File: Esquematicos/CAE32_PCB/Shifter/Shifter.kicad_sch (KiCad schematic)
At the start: 0 parts

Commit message: add: diseño de esquemático básico usando el microcontrolador rp2040
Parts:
- added J1: RJ45, Connector_RJ:RJ45_Amphenol_RJHSE538X, symbol Connector:RJ45
- added J2: USB_C_Receptacle_USB2.0, Connector_USB:USB_C_Receptacle_G-Switch_GT-USB-7010ASV, symbol Connector:USB_C_Receptacle_USB2.0
- added U1: RP2040, Package_DFN_QFN:QFN-56-1EP_7x7mm_P0.4mm_EP3.2x3.2mm, symbol MCU_RaspberryPi:RP2040
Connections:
- new net: U1.1 (IOVDD), U1.10 (IOVDD), U1.22 (IOVDD), U1.33 (IOVDD), U1.42 (IOVDD), U1.49 (IOVDD)
- new net: U1.23 (DVDD), U1.50 (DVDD)
- new net: J2.A1 (GND), J2.A12 (GND), J2.B1 (GND), J2.B12 (GND)
- new net: J2.A4 (VBUS), J2.A9 (VBUS), J2.B4 (VBUS), J2.B9 (VBUS)
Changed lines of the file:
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@@
 (kicad_sch (version 20211123) (generator eeschema)
   (paper "A4")
+  (symbol (lib_id "MCU_RaspberryPi:RP2040") (at 72.39 74.295 0) (unit 1)
+    (in_bom yes) (on_board yes) (fields_autoplaced)
+    (property "Reference" "U1" (id 0) (at 74.4094 119.38 0)
+      (effects (font (size 1.27 1.27)) (justify left))
+    )
+    (property "Value" "RP2040" (id 1) (at 74.4094 121.92 0)
+      (effects (font (size 1.27 1.27)) (justify left))
+    )
+    (property "Footprint" "Package_DFN_QFN:QFN-56-1EP_7x7mm_P0.4mm_EP3.2x3.2mm" (id 2) (at 72.39 74.295 0)
+      (effects (font (size 1.27 1.27)) hide)
+    )
+    (property "Datasheet" "https://datasheets.raspberrypi.com/rp2040/rp2040-datasheet.pdf" (id 3) (at 72.39 74.295 0)
+      (effects (font (size 1.27 1.27)) hide)
+    )
+    (pin "1")
+    (pin "10")
+    (pin "11")
+    (pin "12")
+    (pin "13")
+    (pin "14")
+    (pin "15")
+    (pin "16")
+    (pin "17")
+    (pin "18")
+    (pin "19")
+    (pin "2")
+    (pin "20")
+    (pin "21")
+    (pin "22")
+    (pin "23")
+    (pin "24")
+    (pin "25")
+    (pin "26")
+    (pin "27")
+    (pin "28")
+    (pin "29")
+    (pin "3")
+    (pin "30")
+    (pin "31")
+    (pin "32")
+    (pin "33")
+    (pin "34")
+    (pin "35")
+    (pin "36")
+    (pin "37")
+    (pin "38")
+    (pin "39")
+    (pin "4")
+    (pin "40")
+    (pin "41")
+    (pin "42")
+    (pin "43")
+    (pin "44")
+    (pin "45")
+    (pin "46")
+    (pin "47")
+    (pin "48")
+    (pin "49")
+    (pin "5")
+    (pin "50")
+    (pin "51")
+    (pin "52")
+    (pin "53")
+    (pin "54")
+    (pin "55")
+    (pin "56")
+    (pin "57")
+    (pin "6")
+    (pin "7")
+    (pin "8")
+    (pin "9")
+  )
+  (symbol (lib_id "Connector:RJ45") (at 213.995 41.275 0) (unit 1)
+    (in_bom yes) (on_board yes) (fields_autoplaced)
+    (property "Reference" "J1" (id 0) (at 213.995 22.86 0))
+    (property "Value" "RJ45" (id 1) (at 213.995 25.4 0))
+    (property "Footprint" "Connector_RJ:RJ45_Amphenol_RJHSE538X" (id 2) (at 213.995 40.64 90)
+      (effects (font (size 1.27 1.27)) hide)
+    )
+    (property "Datasheet" "~" (id 3) (at 213.995 40.64 90)
+      (effects (font (size 1.27 1.27)) hide)
+    )
+    (pin "1")
+    (pin "2")
+    (pin "3")
+    (pin "4")
+    (pin "5")
+    (pin "6")
+    (pin "7")
+    (pin "8")
+  )
+  (symbol (lib_id "Connector:USB_C_Receptacle_USB2.0") (at 219.075 83.82 0) (unit 1)
+    (in_bom yes) (on_board yes) (fields_autoplaced)
+    (property "Reference" "J2" (id 0) (at 219.075 60.96 0))
+    (property "Value" "USB_C_Receptacle_USB2.0" (id 1) (at 219.075 63.5 0))
+    (property "Footprint" "Connector_USB:USB_C_Receptacle_G-Switch_GT-USB-7010ASV" (id 2) (at 222.885 83.82 0)
+      (effects (font (size 1.27 1.27)) hide)
+    )
+    (property "Datasheet" "https://www.usb.org/sites/default/files/documents/usb_type-c.zip" (id 3) (at 222.885 83.82 0)
+      (effects (font (size 1.27 1.27)) hide)
+    )
+    (pin "A1")
+    (pin "A12")
+    (pin "A4")
+    (pin "A5")
+    (pin "A6")
+    (pin "A7")
+    (pin "A8")
+    (pin "A9")
+    (pin "B1")
+    (pin "B12")
+    (pin "B4")
+    (pin "B5")
+    (pin "B6")
+    (pin "B7")
+    (pin "B8")
+    (pin "B9")
+    (pin "S1")
+  )
   (sheet_instances
     (path "/" (page "1"))
   )
+  (symbol_instances
+    (path "/d83f6367-21e4-44e4-96ad-633fe7714391"
+      (reference "J1") (unit 1) (value "RJ45") (footprint "Connector_RJ:RJ45_Amphenol_RJHSE538X")
+    )
+    (path "/df924866-e23e-469c-b006-990089a46aff"
+      (reference "J2") (unit 1) (value "USB_C_Receptacle_USB2.0") (footprint "Connector_USB:USB_C_Receptacle_G-Switch_GT-USB-7010ASV")
+    )
+    (path "/5661b59b-f47f-4f9f-b3df-14e1858267dc"
+      (reference "U1") (unit 1) (value "RP2040") (footprint "Package_DFN_QFN:QFN-56-1EP_7x7mm_P0.4mm_EP3.2x3.2mm")
+    )
+  )
 )

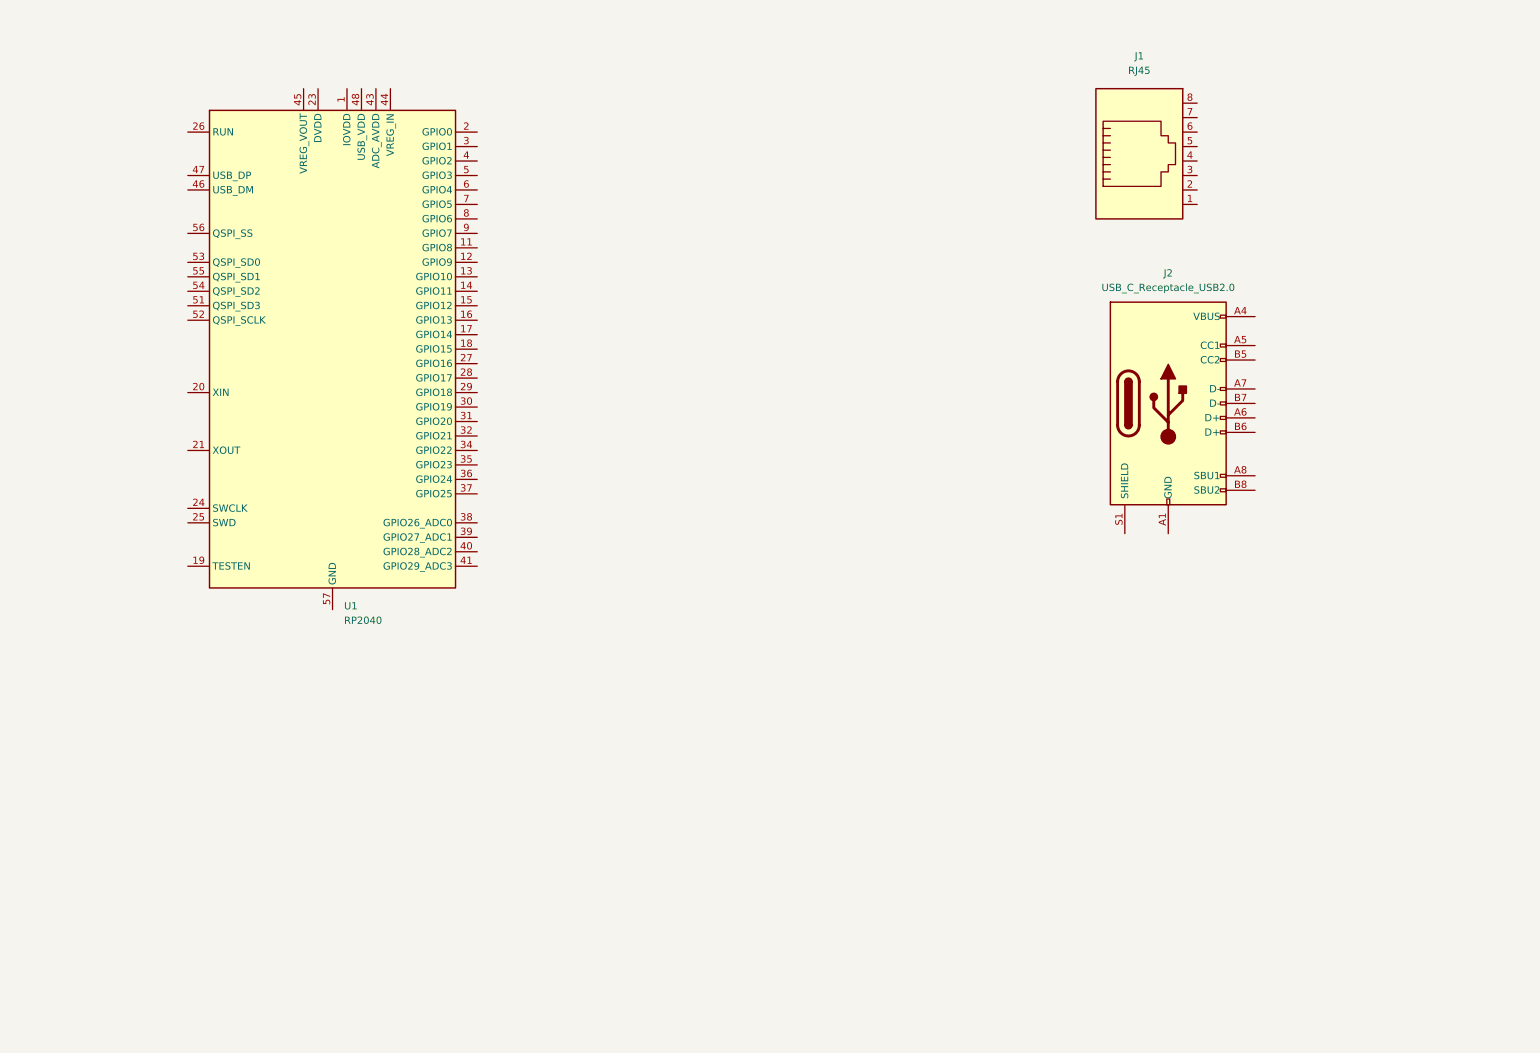
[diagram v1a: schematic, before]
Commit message: update: se enruta completamente la pcb, aunque aun necesario un análisis posterior, ademas de agregar huellas e imagen de la pcb completa
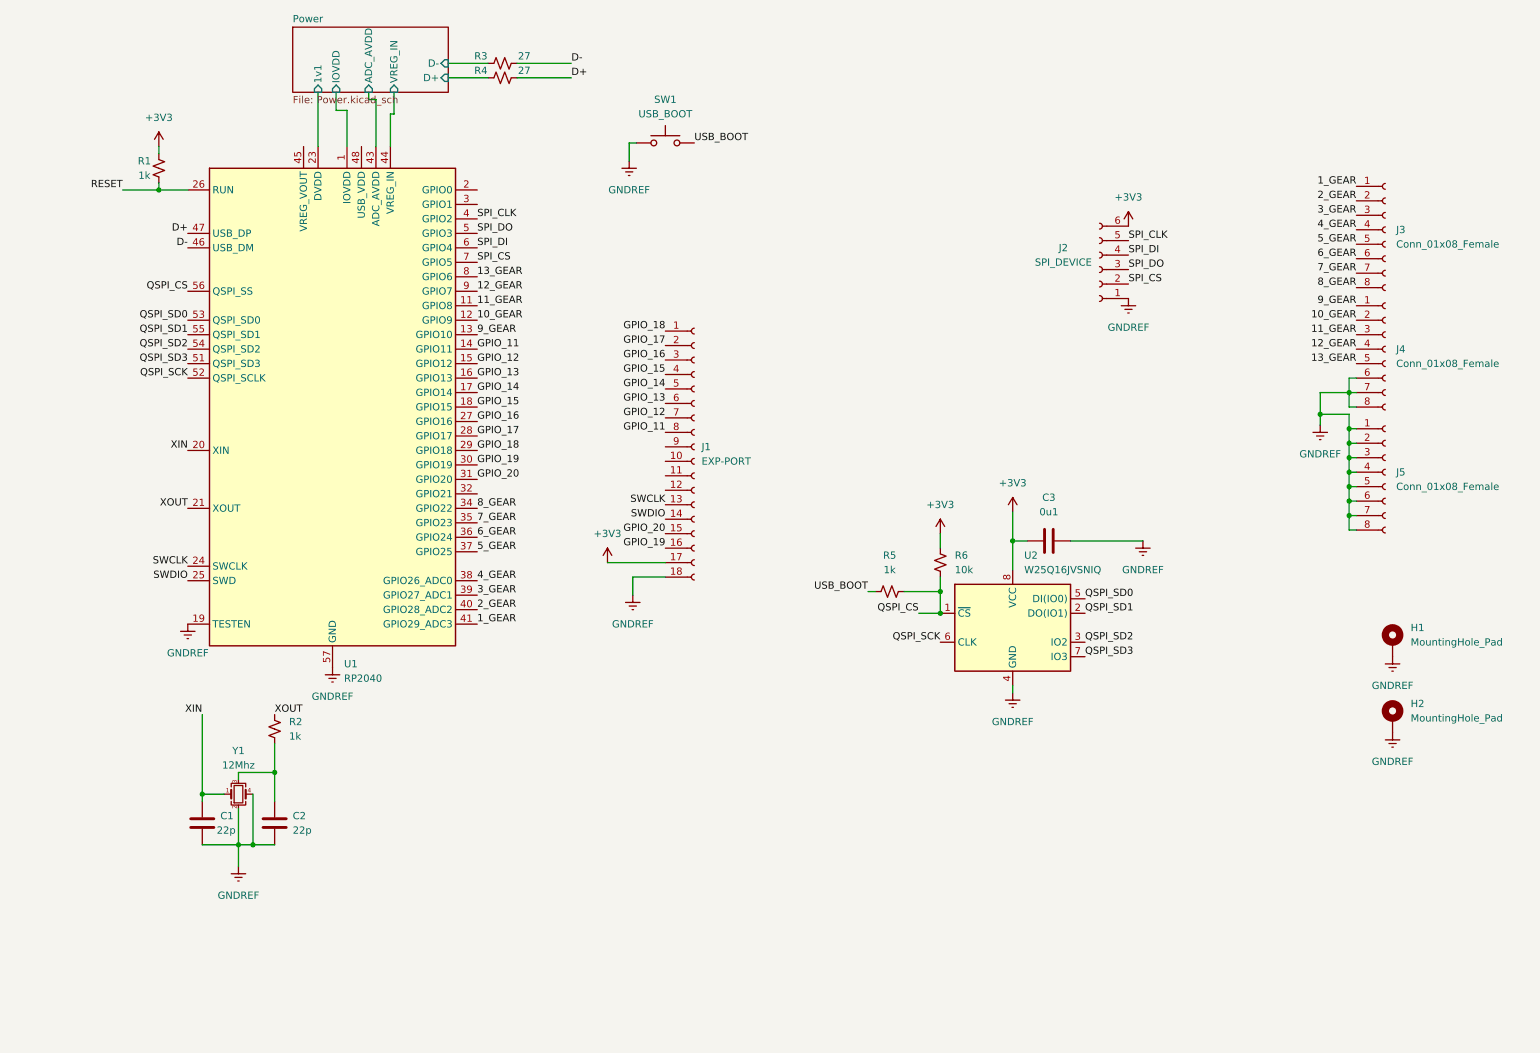
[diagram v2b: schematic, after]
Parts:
- removed J1: RJ45, Connector_RJ:RJ45_Amphenol_RJHSE538X, symbol Connector:RJ45
- removed J2: USB_C_Receptacle_USB2.0, Connector_USB:USB_C_Receptacle_G-Switch_GT-USB-7010ASV, symbol Connector:USB_C_Receptacle_USB2.0
- added C1, C2: 22p, Capacitor_SMD:C_0603_1608Metric_Pad1.08x0.95mm_HandSolder, symbol Device:C
- added C3: 0u1, Capacitor_SMD:C_0603_1608Metric_Pad1.08x0.95mm_HandSolder, symbol Device:C
- added H1, H2: MountingHole_Pad, MountingHole:MountingHole_2.7mm_M2.5_Pad_Via, symbol Mechanical:MountingHole_Pad
- added J1: EXP-PORT, shifter:BM28B0-6-16DS, symbol Connector:Conn_01x18_Female
- added J2: SPI_DEVICE, Connector_PinSocket_2.54mm:PinSocket_2x03_P2.54mm_Vertical, symbol Connector:Conn_01x06_Female
- added J3, J4, J5: Conn_01x08_Female, shifter:shi, symbol Connector:Conn_01x08_Female
- added R1, R2, R5: 1k, Resistor_SMD:R_0603_1608Metric_Pad0.98x0.95mm_HandSolder, symbol Device:R_Small_US
- added R3, R4: 27, Resistor_SMD:R_0603_1608Metric_Pad0.98x0.95mm_HandSolder, symbol Device:R_Small_US
- added R6: 10k, Resistor_SMD:R_0603_1608Metric_Pad0.98x0.95mm_HandSolder, symbol Device:R_Small_US
- added SW1: USB_BOOT, Button_Switch_SMD:SW_Push_SPST_NO_Alps_SKRK, symbol Switch:SW_Push
- added U2: W25Q16JVSNIQ, Package_SO:SOIC-8_5.23x5.23mm_P1.27mm, symbol Memory_Flash:W25Q128JVS
- added Y1: 12Mhz, Crystal:Crystal_SMD_3225-4Pin_3.2x2.5mm, symbol Device:Crystal_GND23_Small
- U1: Vendor (none) -> C2040
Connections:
- net Power/IOVDD: now reaches U1.1 (IOVDD), U1.10 (IOVDD), U1.22 (IOVDD), U1.33 (IOVDD), U1.42 (IOVDD), U1.49 (IOVDD)
- net 11_GEAR: now reaches U1.11 (GPIO8)
- net 11_GEAR: now also J4.3 (Pin_3)
- net 10_GEAR: now reaches U1.12 (GPIO9)
- net 10_GEAR: now also J4.2 (Pin_2)
- net 9_GEAR: now reaches U1.13 (GPIO10)
- net 9_GEAR: now also J4.1 (Pin_1)
- net GPIO_11: now reaches U1.14 (GPIO11)
- net GPIO_11: now also J1.8 (Pin_8)
- net GPIO_12: now reaches U1.15 (GPIO12)
- net GPIO_12: now also J1.7 (Pin_7)
- net GPIO_13: now reaches U1.16 (GPIO13)
- net GPIO_13: now also J1.6 (Pin_6)
- net GPIO_14: now reaches U1.17 (GPIO14)
- net GPIO_14: now also J1.5 (Pin_5)
- net GPIO_15: now reaches U1.18 (GPIO15)
- net GPIO_15: now also J1.4 (Pin_4)
- net GNDREF: now reaches U1.19 (TESTEN)
- net GNDREF: now also U1.57 (GND), C1.2, C2.2, C3.2, H1.1, H2.1, J1.18 (Pin_18), J2.1 (Pin_1), J4.6 (Pin_6), J4.7 (Pin_7), J4.8 (Pin_8), J5.1 (Pin_1), J5.2 (Pin_2), J5.3 (Pin_3), J5.4 (Pin_4), J5.5 (Pin_5), J5.6 (Pin_6), J5.7 (Pin_7), J5.8 (Pin_8), SW1.1, U2.4 (GND), Y1.2, Y1.4
- net XIN: now reaches U1.20 (XIN)
- net XIN: now also C1.1, Y1.1
- net XOUT: now reaches U1.21 (XOUT)
- net XOUT: now also R2.1
- net Power/1v1: now reaches U1.23 (DVDD), U1.50 (DVDD)
- net SWCLK: now reaches U1.24 (SWCLK)
- net SWCLK: now also J1.13 (Pin_13)
- net SWDIO: now reaches U1.25 (SWD)
- net SWDIO: now also J1.14 (Pin_14)
- net RESET: now reaches U1.26 (RUN)
- net RESET: now also R1.2
- net GPIO_16: now reaches U1.27 (GPIO16)
- net GPIO_16: now also J1.3 (Pin_3)
- net GPIO_17: now reaches U1.28 (GPIO17)
- net GPIO_17: now also J1.2 (Pin_2)
- net GPIO_18: now reaches U1.29 (GPIO18)
- net GPIO_18: now also J1.1 (Pin_1)
- net GPIO_19: now reaches U1.30 (GPIO19)
- net GPIO_19: now also J1.16 (Pin_16)
- net GPIO_20: now reaches U1.31 (GPIO20)
- net GPIO_20: now also J1.15 (Pin_15)
- net 8_GEAR: now reaches U1.34 (GPIO22)
- net 8_GEAR: now also J3.8 (Pin_8)
- net 7_GEAR: now reaches U1.35 (GPIO23)
- net 7_GEAR: now also J3.7 (Pin_7)
- net 6_GEAR: now reaches U1.36 (GPIO24)
- net 6_GEAR: now also J3.6 (Pin_6)
- net 5_GEAR: now reaches U1.37 (GPIO25)
- net 5_GEAR: now also J3.5 (Pin_5)
- net 4_GEAR: now reaches U1.38 (GPIO26_ADC0)
- net 4_GEAR: now also J3.4 (Pin_4)
- net 3_GEAR: now reaches U1.39 (GPIO27_ADC1)
- net 3_GEAR: now also J3.3 (Pin_3)
- net SPI_CLK: now reaches U1.4 (GPIO2)
- net SPI_CLK: now also J2.5 (Pin_5)
- net 2_GEAR: now reaches U1.40 (GPIO28_ADC2)
- net 2_GEAR: now also J3.2 (Pin_2)
- net 1_GEAR: now reaches U1.41 (GPIO29_ADC3)
- net 1_GEAR: now also J3.1 (Pin_1)
- net Power/ADC_AVDD: now reaches U1.43 (ADC_AVDD)
- net Power/VREG_IN: now reaches U1.44 (VREG_IN)
- net D-: now reaches U1.46 (USB_DM)
- net D-: now also R3.1
- net D+: now reaches U1.47 (USB_DP)
- net D+: now also R4.1
- net SPI_DO: now reaches U1.5 (GPIO3)
- net SPI_DO: now also J2.3 (Pin_3)
- net QSPI_SD3: now reaches U1.51 (QSPI_SD3)
- net QSPI_SD3: now also U2.7 (IO3)
- net QSPI_SCK: now reaches U1.52 (QSPI_SCLK)
- net QSPI_SCK: now also U2.6 (CLK)
- net QSPI_SD0: now reaches U1.53 (QSPI_SD0)
- net QSPI_SD0: now also U2.5 (DI(IO0))
- net QSPI_SD2: now reaches U1.54 (QSPI_SD2)
- net QSPI_SD2: now also U2.3 (IO2)
- net QSPI_SD1: now reaches U1.55 (QSPI_SD1)
- net QSPI_SD1: now also U2.2 (DO(IO1))
- net QSPI_CS: now reaches U1.56 (QSPI_SS)
- net QSPI_CS: now also R5.2, R6.1, U2.1 (~{CS})
- net SPI_DI: now reaches U1.6 (GPIO4)
- net SPI_DI: now also J2.4 (Pin_4)
- net SPI_CS: now reaches U1.7 (GPIO5)
- net SPI_CS: now also J2.2 (Pin_2)
- net 13_GEAR: now reaches U1.8 (GPIO6)
- net 13_GEAR: now also J4.5 (Pin_5)
- net 12_GEAR: now reaches U1.9 (GPIO7)
- net 12_GEAR: now also J4.4 (Pin_4)
- new net: C2.1, R2.2, Y1.3
- new net +3V3: C3.1, J1.17 (Pin_17), J2.6 (Pin_6), R1.1, R6.2, U2.8 (VCC)
- new net Power/D+: R4.2
- new net Power/D-: R3.2
- new net USB_BOOT: R5.1, SW1.2
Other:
- added sheet Power (Power.kicad_sch)
- moved on the sheet: U1

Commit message: update:Shifter PCB v1.1 Revision 1: Se cambia la posición de los "castelladed pins" a un solo lado, aumentando un poco el tamaño de la pcb pero reduciendo el costo de manufactura, ademas se añade la serigrafia correspondiente a la PCB
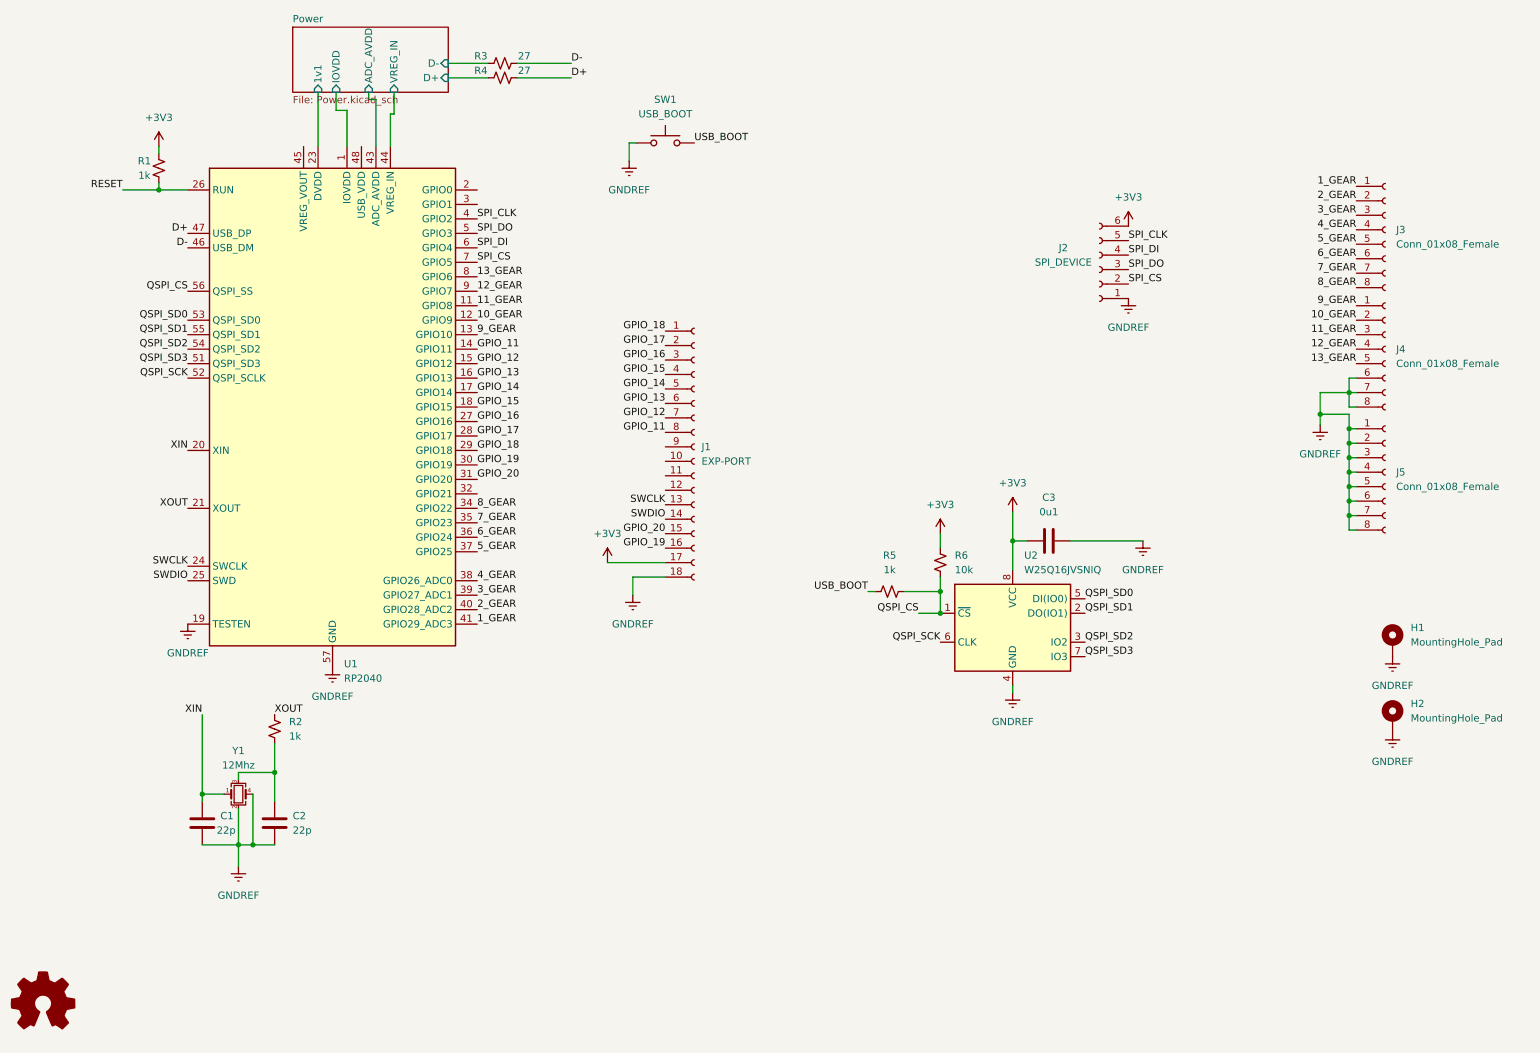
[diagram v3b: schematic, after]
